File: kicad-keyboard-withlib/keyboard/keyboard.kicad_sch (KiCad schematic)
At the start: 47 parts, among them SW1 SW_Push, SW10 SW_Push, SW11 SW_Push, SW12 SW_Push, SW13 SW_Push, SW14 SW_Push, SW15 SW_Push, SW16 SW_Push, SW17 SW_Push, SW18 SW_Push, SW19 SW_Push, SW2 SW_Push, SW20 SW_Push, SW21 SW_Push, SW22 SW_Push, SW23 SW_Push, SW24 SW_Push, SW25 SW_Push, SW26 SW_Push, SW27 SW_Push, SW28 SW_Push, SW29 SW_Push, SW3 SW_Push, SW30 SW_Push, SW31 SW_Push, SW32 SW_Push, SW33 SW_Push, SW34 SW_Push, SW35 SW_Push, SW36 SW_Push, SW37 SW_Push, SW38 SW_Push, SW39 SW_Slide_DPDT, SW4 SW_Push, SW5 SW_Push, SW6 SW_Push, SW7 SW_Push, SW8 SW_Push, SW9 SW_Push, U2 MCP23017_SO

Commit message: add: footprint for slide switch and added it to pcb
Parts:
- SW39: footprint Button_Switch_THT:SW_CK_JS202011CQN_DPDT_Straight -> Lilyspad:slide_switch
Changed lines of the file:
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@@
 			)
 		)
-		(property "Footprint" "Button_Switch_THT:SW_CK_JS202011CQN_DPDT_Straight"
+		(property "Footprint" "Lilyspad:slide_switch"
 			(at 175.26 63.5 0)
 			(effects

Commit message: add: all footprint done, pcb with own footprint, to finish
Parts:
- SW1, SW10, SW11, SW12, SW13, SW14, SW15, SW16, SW17, SW18, SW19, SW2, SW20, SW21, SW22, SW23, SW24, SW25, SW26, SW27, SW28, SW29, SW3, SW30, SW31, SW32, SW33, SW34, SW35, SW36, SW37, SW38, SW4, SW5, SW6, SW7, SW8, SW9: footprint Button_Switch_THT:SW_PUSH-12mm_Wuerth-430476085716 -> Lilyspad:push_switch
- SW40: footprint (none) -> Lilyspad:rotary_encoder
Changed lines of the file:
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@@
 			)
 		)
-		(property "Footprint" "Button_Switch_THT:SW_PUSH-12mm_Wuerth-430476085716"
+		(property "Footprint" "Lilyspad:push_switch"
 			(at 88.9 121.92 0)
 			(effects
@@
 			)
 		)
-		(property "Footprint" "Button_Switch_THT:SW_PUSH-12mm_Wuerth-430476085716"
+		(property "Footprint" "Lilyspad:push_switch"
 			(at 73.66 144.78 0)
 			(effects
@@
 			)
 		)
-		(property "Footprint" "Button_Switch_THT:SW_PUSH-12mm_Wuerth-430476085716"
+		(property "Footprint" "Lilyspad:push_switch"
 			(at 88.9 97.79 0)
 			(effects
@@
 			)
 		)
-		(property "Footprint" "Button_Switch_THT:SW_PUSH-12mm_Wuerth-430476085716"
+		(property "Footprint" "Lilyspad:push_switch"
 			(at 43.18 168.91 0)
 			(effects
@@
 			)
 		)
-		(property "Footprint" "Button_Switch_THT:SW_PUSH-12mm_Wuerth-430476085716"
+		(property "Footprint" "Lilyspad:push_switch"
 			(at 43.18 121.92 0)
 			(effects
@@
 			)
 		)
-		(property "Footprint" "Button_Switch_THT:SW_PUSH-12mm_Wuerth-430476085716"
+		(property "Footprint" "Lilyspad:push_switch"
 			(at 149.86 97.79 0)
 			(effects
@@
 			)
 		)
-		(property "Footprint" "Button_Switch_THT:SW_PUSH-12mm_Wuerth-430476085716"
+		(property "Footprint" "Lilyspad:push_switch"
 			(at 88.9 168.91 0)
 			(effects
@@
 			)
 		)
-		(property "Footprint" "Button_Switch_THT:SW_PUSH-12mm_Wuerth-430476085716"
+		(property "Footprint" "Lilyspad:push_switch"
 			(at 43.18 97.79 0)
 			(effects
@@
 			)
 		)
-		(property "Footprint" "Button_Switch_THT:SW_PUSH-12mm_Wuerth-430476085716"
+		(property "Footprint" "Lilyspad:push_switch"
 			(at 149.86 144.78 0)
 			(effects
@@
 			)
 		)
-		(property "Footprint" "Button_Switch_THT:SW_PUSH-12mm_Wuerth-430476085716"
+		(property "Footprint" "Lilyspad:push_switch"
 			(at 58.42 121.92 0)
 			(effects
@@
 			)
 		)
-		(property "Footprint" "Button_Switch_THT:SW_PUSH-12mm_Wuerth-430476085716"
+		(property "Footprint" "Lilyspad:push_switch"
 			(at 104.14 168.91 0)
 			(effects
@@
 			)
 		)
-		(property "Footprint" "Button_Switch_THT:SW_PUSH-12mm_Wuerth-430476085716"
+		(property "Footprint" "Lilyspad:push_switch"
 			(at 119.38 168.91 0)
 			(effects
@@
 			)
 		)
-		(property "Footprint" "Button_Switch_THT:SW_PUSH-12mm_Wuerth-430476085716"
+		(property "Footprint" "Lilyspad:push_switch"
 			(at 73.66 121.92 0)
 			(effects
@@
 			)
 		)
-		(property "Footprint" "Button_Switch_THT:SW_PUSH-12mm_Wuerth-430476085716"
+		(property "Footprint" "Lilyspad:push_switch"
 			(at 165.1 97.79 0)
 			(effects
@@
 			)
 		)
-		(property "Footprint" "Button_Switch_THT:SW_PUSH-12mm_Wuerth-430476085716"
+		(property "Footprint" "Lilyspad:push_switch"
 			(at 58.42 168.91 0)
 			(effects
@@
 			)
 		)
-		(property "Footprint" "Button_Switch_THT:SW_PUSH-12mm_Wuerth-430476085716"
+		(property "Footprint" "Lilyspad:push_switch"
 			(at 27.94 144.78 0)
 			(effects
@@
 			)
 		)
-		(property "Footprint" "Button_Switch_THT:SW_PUSH-12mm_Wuerth-430476085716"
+		(property "Footprint" "Lilyspad:push_switch"
 			(at 27.94 168.91 0)
 			(effects
@@
 			)
 		)
-		(property "Footprint" "Button_Switch_THT:SW_PUSH-12mm_Wuerth-430476085716"
+		(property "Footprint" "Lilyspad:push_switch"
 			(at 119.38 144.78 0)
 			(effects
@@
 			)
 		)
-		(property "Footprint" "Button_Switch_THT:SW_PUSH-12mm_Wuerth-430476085716"
+		(property "Footprint" "Lilyspad:push_switch"
 			(at 134.62 97.79 0)
 			(effects
@@
 			)
 		)
-		(property "Footprint" "Button_Switch_THT:SW_PUSH-12mm_Wuerth-430476085716"
+		(property "Footprint" "Lilyspad:push_switch"
 			(at 27.94 121.92 0)
 			(effects
@@
 			)
 		)
-		(property "Footprint" "Button_Switch_THT:SW_PUSH-12mm_Wuerth-430476085716"
+		(property "Footprint" "Lilyspad:push_switch"
 			(at 88.9 144.78 0)
 			(effects
@@
 			)
 		)
-		(property "Footprint" "Button_Switch_THT:SW_PUSH-12mm_Wuerth-430476085716"
+		(property "Footprint" "Lilyspad:push_switch"
 			(at 104.14 144.78 0)
 			(effects
@@
 			)
 		)
-		(property "Footprint" "Button_Switch_THT:SW_PUSH-12mm_Wuerth-430476085716"
+		(property "Footprint" "Lilyspad:push_switch"
 			(at 104.14 97.79 0)
 			(effects
@@
 			)
 		)
-		(property "Footprint" "Button_Switch_THT:SW_PUSH-12mm_Wuerth-430476085716"
+		(property "Footprint" "Lilyspad:push_switch"
 			(at 165.1 144.78 0)
 			(effects
@@
 			)
 		)
-		(property "Footprint" "Button_Switch_THT:SW_PUSH-12mm_Wuerth-430476085716"
+		(property "Footprint" "Lilyspad:push_switch"
 			(at 27.94 97.79 0)
 			(effects
@@
 			)
 		)
-		(property "Footprint" "Button_Switch_THT:SW_PUSH-12mm_Wuerth-430476085716"
+		(property "Footprint" "Lilyspad:push_switch"
 			(at 119.38 97.79 0)
 			(effects
@@
 			)
 		)
-		(property "Footprint" "Button_Switch_THT:SW_PUSH-12mm_Wuerth-430476085716"
+		(property "Footprint" "Lilyspad:push_switch"
 			(at 73.66 168.91 0)
 			(effects
@@
 			)
 		)
-		(property "Footprint" "Button_Switch_THT:SW_PUSH-12mm_Wuerth-430476085716"
+		(property "Footprint" "Lilyspad:push_switch"
 			(at 73.66 97.79 0)
 			(effects
@@
 			)
 		)
-		(property "Footprint" "Button_Switch_THT:SW_PUSH-12mm_Wuerth-430476085716"
+		(property "Footprint" "Lilyspad:push_switch"
 			(at 149.86 121.92 0)
 			(effects
@@
 			)
 		)
-		(property "Footprint" "Button_Switch_THT:SW_PUSH-12mm_Wuerth-430476085716"
+		(property "Footprint" "Lilyspad:push_switch"
 			(at 58.42 144.78 0)
 			(effects
@@
 			)
 		)
-		(property "Footprint" "Button_Switch_THT:SW_PUSH-12mm_Wuerth-430476085716"
+		(property "Footprint" "Lilyspad:push_switch"
 			(at 119.38 121.92 0)
 			(effects
@@
 			)
 		)
-		(property "Footprint" "Button_Switch_THT:SW_PUSH-12mm_Wuerth-430476085716"
+		(property "Footprint" "Lilyspad:push_switch"
 			(at 134.62 121.92 0)
 			(effects
@@
 			)
 		)
-		(property "Footprint" "Button_Switch_THT:SW_PUSH-12mm_Wuerth-430476085716"
+		(property "Footprint" "Lilyspad:push_switch"
 			(at 134.62 168.91 0)
 			(effects
@@
 			)
 		)
-		(property "Footprint" "Button_Switch_THT:SW_PUSH-12mm_Wuerth-430476085716"
+		(property "Footprint" "Lilyspad:push_switch"
 			(at 58.42 97.79 0)
 			(effects
@@
 			)
 		)
-		(property "Footprint" "Button_Switch_THT:SW_PUSH-12mm_Wuerth-430476085716"
+		(property "Footprint" "Lilyspad:push_switch"
 			(at 134.62 144.78 0)
 			(effects
@@
 			)
 		)
-		(property "Footprint" "Button_Switch_THT:SW_PUSH-12mm_Wuerth-430476085716"
+		(property "Footprint" "Lilyspad:push_switch"
 			(at 104.14 121.92 0)
 			(effects
@@
 			)
 		)
-		(property "Footprint" "Button_Switch_THT:SW_PUSH-12mm_Wuerth-430476085716"
+		(property "Footprint" "Lilyspad:push_switch"
 			(at 165.1 121.92 0)
 			(effects
@@
 					(size 1.27 1.27)
 				)
+				(hide yes)
 			)
 		)
-		(property "Footprint" ""
+		(property "Footprint" "Lilyspad:rotary_encoder"
 			(at 261.62 100.33 0)
 			(effects
@@
 			)
 		)
-		(property "Footprint" "Button_Switch_THT:SW_PUSH-12mm_Wuerth-430476085716"
+		(property "Footprint" "Lilyspad:push_switch"
 			(at 43.18 144.78 0)
 			(effects

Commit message: no more rotary pb
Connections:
- net GND: now also SW40.D; no longer SW40.S1
- net at U2.26 (GPA5): now also SW40.E; no longer SW40.S2
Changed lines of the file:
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@@
 		(pin "C"
 		)
-		(pin "S2"
+		(pin "D"
 		)
 		(pin "B"
 		)
-		(pin "S1"
+		(pin "E"
 		)
 		(pin "A"

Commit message: add: new male header
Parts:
- removed P1: ~, Lilyspad:pin_socket, symbol Lilyspad:pin_socket
- added U1: ~, Lilyspad:male_header, symbol Lilyspad:header_26
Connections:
- net GND: now also U1.15 (GND)
- net VCC: now also U1.16 (VCC)
- net at SW11.1, SW12.1, SW13.1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: now also U1.2 (R2)
- net at SW15.2, SW25.2, SW35.2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: now also U1.9 (C5)
- net at SW21.1, SW22.1, SW23.1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: now also U1.3 (R3)
- net at SW14.2, SW24.2, SW34.2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: now also U1.8 (C4)
- net at SW1.1, SW10.1, SW2.1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: now also U1.1 (R1)
- net at SW31.1, SW32.1, SW33.1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: now also U1.4 (R4)
- net at SW12.2, SW2.2, SW22.2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: now also U1.6 (C2)
- net at SW19.2, SW29.2, SW9.2: now also U1.13 (C9)
- net at R3.2, U2.13 (SDA): now also U1.20 (SDA)
- net at R2.2, U2.12 (SCK): now also U1.21 (SCL)
- net at SW13.2, SW23.2, SW3.2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: now also U1.7 (C3)
- net at SW16.2, SW26.2, SW36.2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: now also U1.10 (C6)
- net at SW17.2, SW27.2, SW37.2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: now also U1.11 (C7)
- net at SW10.2, SW20.2, SW30.2: now also U1.14 (C10)
- net at SW1.2, SW11.2, SW21.2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: now also U1.5 (C1)
- net at SW18.2, SW28.2, SW38.2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: now also U1.12 (C8)
- net at SW39.1 (A): now also U1.17 (SLD_SW)
- net at SW39.2 (B): now also U1.18 (SLD_SW)
- net at SW39.3 (C): now also U1.19 (SLD_SW)
- no-connect marks 18 -> 23
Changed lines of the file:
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@@
 	)
 	(no_connect
+		(at 180.34 27.94)
+	)
+	(no_connect
 		(at 240.03 124.46)
 	)
@@
 	)
 	(no_connect
+		(at 182.88 27.94)
+	)
+	(no_connect
 		(at 240.03 104.14)
 	)
@@
 	)
 	(no_connect
+		(at 177.8 27.94)
+	)
+	(no_connect
 		(at 240.03 121.92)
 	)
@@
 	)
 	(no_connect
+		(at 172.72 27.94)
+	)
+	(no_connect
+		(at 175.26 27.94)
+	)
+	(no_connect
 		(at 204.47 109.22)
 	)
@@
 	)
 	(symbol
-		(lib_id "Switch:SW_Push")
-		(at 119.38 102.87 0)
+		(lib_id "Lilyspad:header_26")
+		(at 116.84 24.13 90)
 		(unit 1)
 		(exclude_from_sim no)
@@
 		(dnp no)
 		(fields_autoplaced yes)
-		(property "Reference" "SW7"
-			(at 119.38 95.25 0)
+		(property "Reference" "U1"
+			(at 151.257 15.24 90)
 			(effects
 				(font
@@
 			)
 		)
-		(property "Value" "SW_Push"
-			(at 119.38 97.79 0)
+		(property "Value" "~"
+			(at 151.257 17.78 90)
 			(effects
 				(font
@@
 			)
 		)
-		(property "Footprint" "Lilyspad:push_switch"
-			(at 119.38 97.79 0)
+		(property "Footprint" "Lilyspad:male_header"
+			(at 116.84 24.13 0)
 			(effects
 				(font
@@
 			)
 		)
-		(property "Datasheet" "~"
-			(at 119.38 97.79 0)
+		(property "Datasheet" ""
+			(at 116.84 24.13 0)
 			(effects
 				(font
@@
 			)
 		)
-		(property "Description" "Push button switch, generic, two pins"
-			(at 119.38 102.87 0)
+		(property "Description" ""
+			(at 116.84 24.13 0)
 			(effects
 				(font
@@
 			)
 		)
-		(pin "1"
+		(pin "8"
+		)
+		(pin "3"
+		)
+		(pin "13"
+		)
+		(pin "11"
+		)
+		(pin "21"
+		)
+		(pin "22"
+		)
+		(pin "19"
+		)
+		(pin "20"
+		)
+		(pin "17"
+		)
+		(pin "5"
 		)
 		(pin "2"
 		)
+		(pin "4"
+		)
+		(pin "23"
+		)
+		(pin "24"
+		)
+		(pin "14"
+		)
+		(pin "1"
+		)
+		(pin "7"
+		)
+		(pin "6"
+		)
+		(pin "10"
+		)
+		(pin "16"
+		)
+		(pin "12"
+		)
+		(pin "9"
+		)
+		(pin "26"
+		)
+		(pin "15"
+		)
+		(pin "25"
+		)
+		(pin "18"
+		)
 		(instances
-			(project "keyboard"
+			(project ""
 				(path "/55764147-763c-452f-85b8-3be2d22c3190"
-					(reference "SW7")
+					(reference "U1")
 					(unit 1)
 				)
@@
 	)
 	(symbol
-		(lib_id "Lilyspad:pin_socket")
-		(at 116.84 25.4 90)
+		(lib_id "Switch:SW_Push")
+		(at 119.38 102.87 0)
 		(unit 1)
 		(exclude_from_sim no)
@@
 		(dnp no)
 		(fields_autoplaced yes)
-		(property "Reference" "P1"
-			(at 144.907 15.24 90)
+		(property "Reference" "SW7"
+			(at 119.38 95.25 0)
 			(effects
 				(font
@@
 			)
 		)
-		(property "Value" "~"
-			(at 144.907 17.78 90)
+		(property "Value" "SW_Push"
+			(at 119.38 97.79 0)
 			(effects
 				(font
 					(size 1.27 1.27)
 				)
-				(hide yes)
 			)
 		)
-		(property "Footprint" "Lilyspad:pin_socket"
-			(at 116.84 25.4 0)
+		(property "Footprint" "Lilyspad:push_switch"
+			(at 119.38 97.79 0)
 			(effects
 				(font
@@
 			)
 		)
-		(property "Datasheet" ""
-			(at 116.84 25.4 0)
+		(property "Datasheet" "~"
+			(at 119.38 97.79 0)
 			(effects
 				(font
@@
 			)
 		)
-		(property "Description" ""
-			(at 116.84 25.4 0)
+		(property "Description" "Push button switch, generic, two pins"
+			(at 119.38 102.87 0)
 			(effects
 				(font
@@
 			)
 		)
-		(pin "9"
-		)
-		(pin "2"
-		)
-		(pin "16"
-		)
-		(pin "13"
-		)
-		(pin "12"
-		)
-		(pin "14"
-		)
-		(pin "21"
-		)
-		(pin "19"
-		)
-		(pin "4"
-		)
-		(pin "5"
-		)
 		(pin "1"
 		)
-		(pin "11"
-		)
-		(pin "15"
-		)
-		(pin "20"
-		)
-		(pin "17"
-		)
-		(pin "10"
-		)
-		(pin "6"
-		)
-		(pin "7"
-		)
-		(pin "8"
-		)
-		(pin "18"
-		)
-		(pin "3"
+		(pin "2"
 		)
 		(instances
-			(project ""
+			(project "keyboard"
 				(path "/55764147-763c-452f-85b8-3be2d22c3190"
-					(reference "P1")
+					(reference "SW7")
 					(unit 1)
 				)

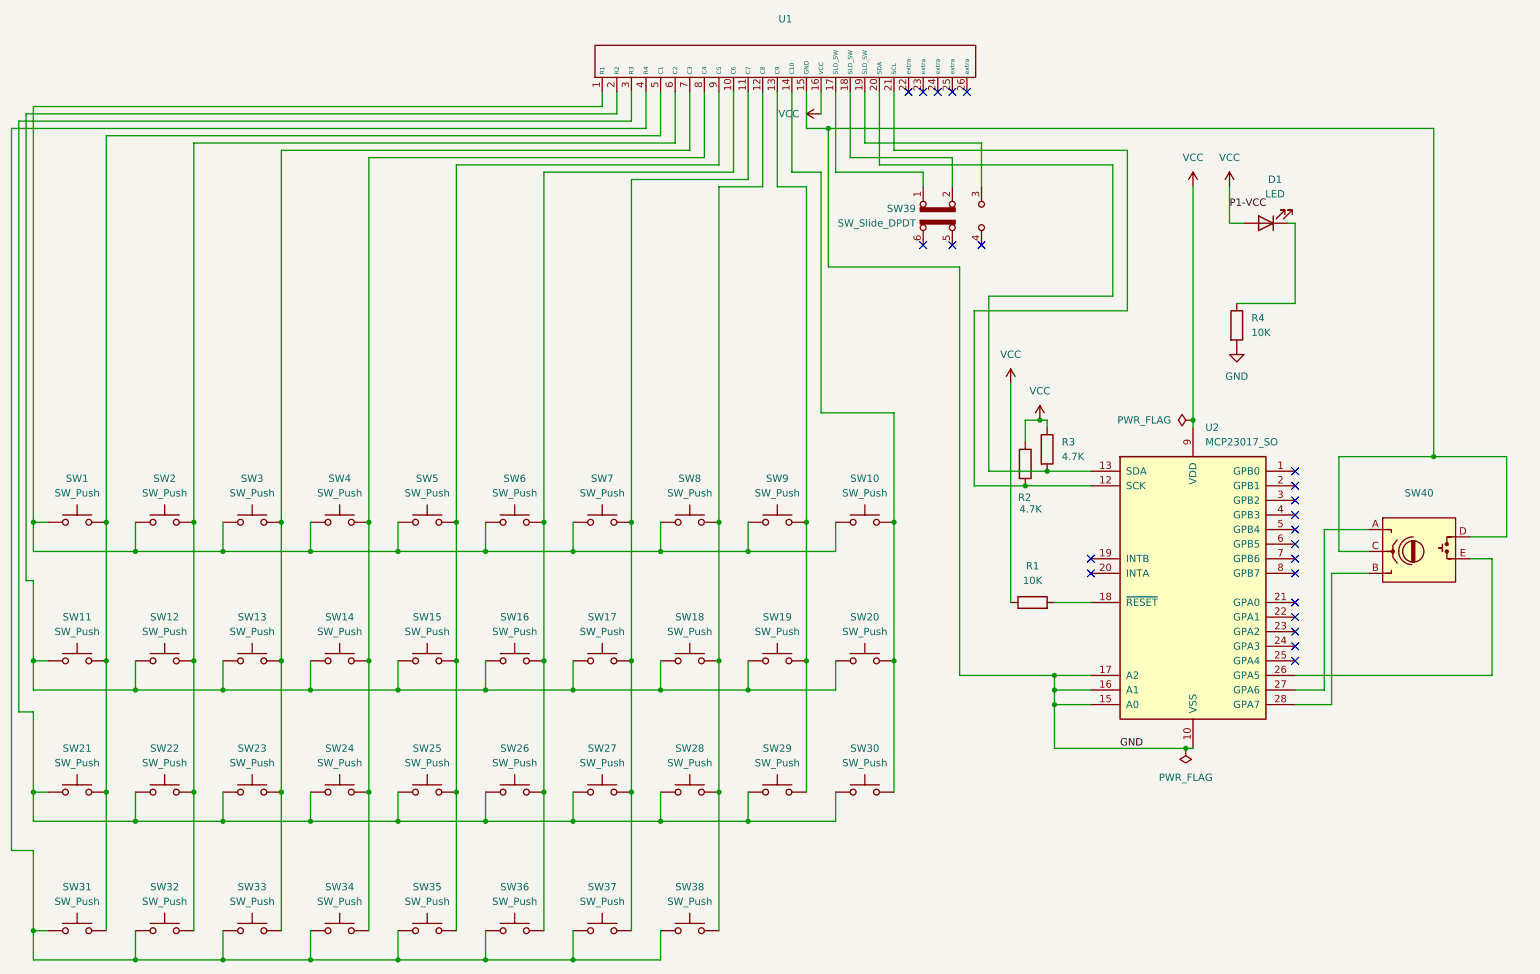
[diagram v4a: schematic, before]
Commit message: add: symbole and footprint for diode, schematic has diode now
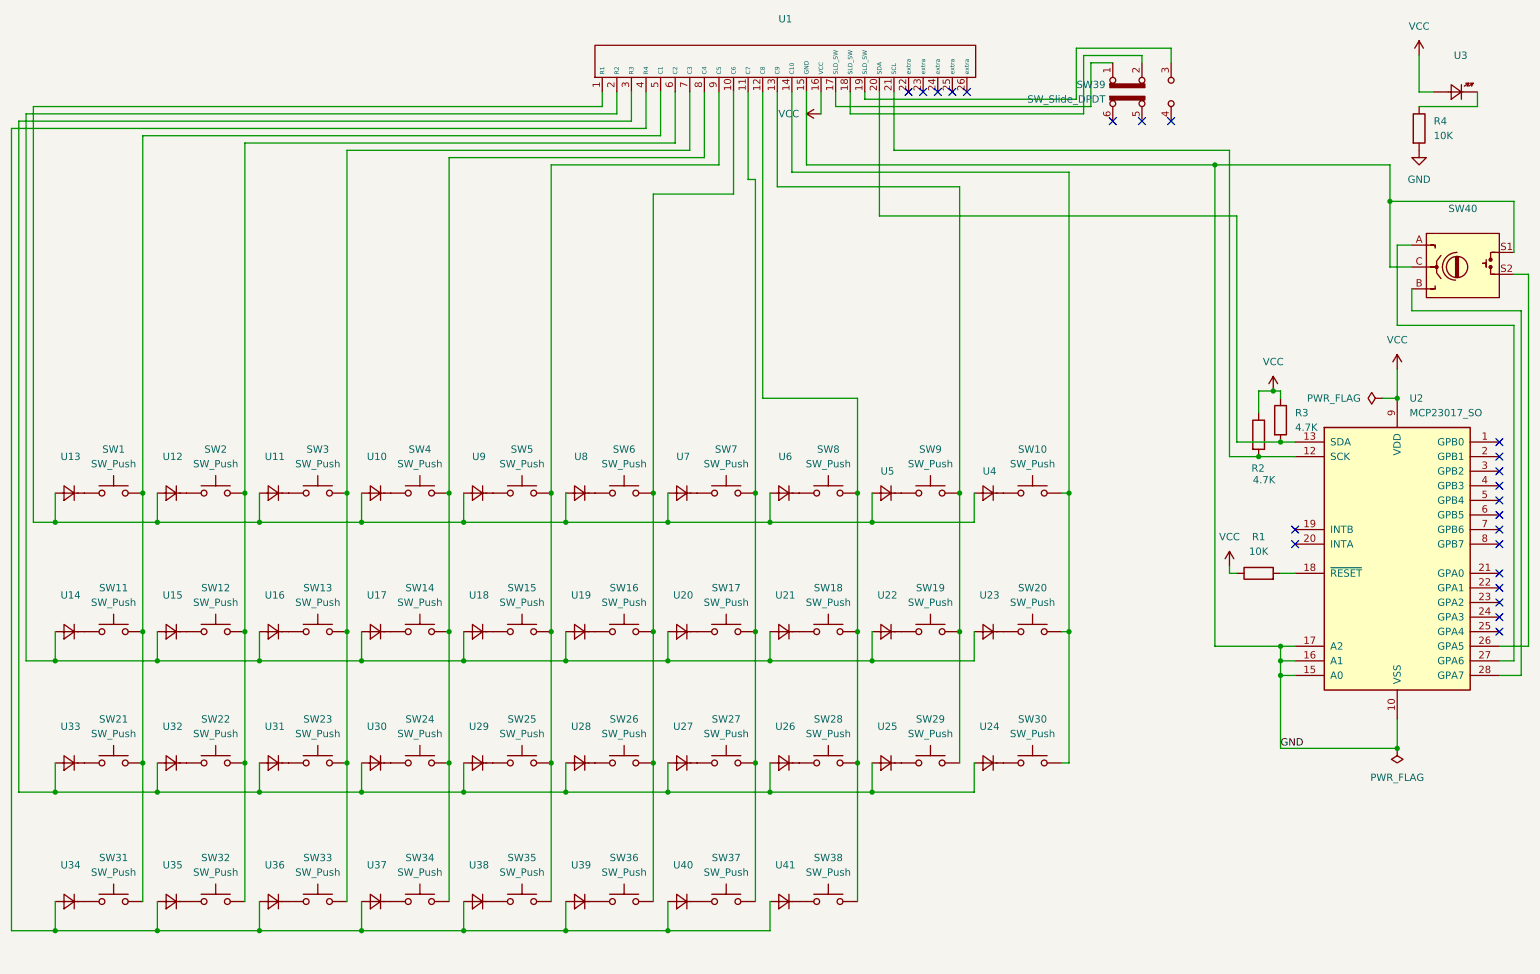
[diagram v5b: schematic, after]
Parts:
- removed D1: LED, Lilyspad:led, symbol Device:LED
- added U10, U11, U12, U13, U14, U15, U16, U17, U18, U19, U20, U21, U22, U23, U24, U25, U26, U27, U28, U29, U30, U31, U32, U33, U34, U35, U36, U37, U38, U39, U4, U40, U41, U5, U6, U7, U8, U9: ~, symbol Lilyspad:diode
- added U3: ~, symbol Lilyspad:led
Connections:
- net GND: now also SW40.S1; no longer SW40.D
- net VCC: now also U3.1
- net at R4.1: now also U3.2
- net at U2.26 (GPA5): now also SW40.S2; no longer SW40.E
- new net: SW15.1, U18.1
- new net: SW13.1, U16.1
- new net: U1.2 (R2), U14.2, U15.2, U16.2, U17.2, U18.2, U19.2, U20.2, U21.2, U22.2, U23.2
- new net: SW28.1, U26.1
- new net: U1.3 (R3), U24.2, U25.2, U26.2, U27.2, U28.2, U29.2, U30.2, U31.2, U32.2, U33.2
- new net: SW24.1, U30.1
- new net: SW20.1, U23.1
- new net: SW26.1, U28.1
- new net: SW5.1, U9.1
- new net: SW32.1, U35.1
- new net: SW4.1, U10.1
- new net: U1.1 (R1), U10.2, U11.2, U12.2, U13.2, U4.2, U5.2, U6.2, U7.2, U8.2, U9.2
- new net: SW12.1, U15.1
- new net: SW9.1, U5.1
- new net: SW35.1, U38.1
- new net: SW19.1, U22.1
- new net: SW2.1, U12.1
- new net: SW36.1, U39.1
- new net: U1.4 (R4), U34.2, U35.2, U36.2, U37.2, U38.2, U39.2, U40.2, U41.2
- new net: SW30.1, U24.1
- new net: SW22.1, U32.1
- new net: SW38.1, U41.1
- new net: SW33.1, U36.1
- new net: SW29.1, U25.1
- new net: SW37.1, U40.1
- new net: SW14.1, U17.1
- new net: SW10.1, U4.1
- new net: SW21.1, U33.1
- new net: SW31.1, U34.1
- new net: SW27.1, U27.1
- new net: SW8.1, U6.1
- new net: SW11.1, U14.1
- new net: SW25.1, U29.1
- new net: SW6.1, U8.1
- new net: SW1.1, U13.1
- new net: SW7.1, U7.1
- new net: SW3.1, U11.1
- new net: SW34.1, U37.1
- new net: SW23.1, U31.1
- new net: SW17.1, U20.1
- new net: SW18.1, U21.1
- new net: SW16.1, U19.1
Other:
- moved on the sheet: R1, R2, R3, R4, SW1, SW10, SW11, SW12, SW13, SW14, SW15, SW16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
